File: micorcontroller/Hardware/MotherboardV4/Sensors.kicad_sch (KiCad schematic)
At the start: 36 parts, among them IC5 MS561101BA03-50, U1 TLV9002QDRQ1

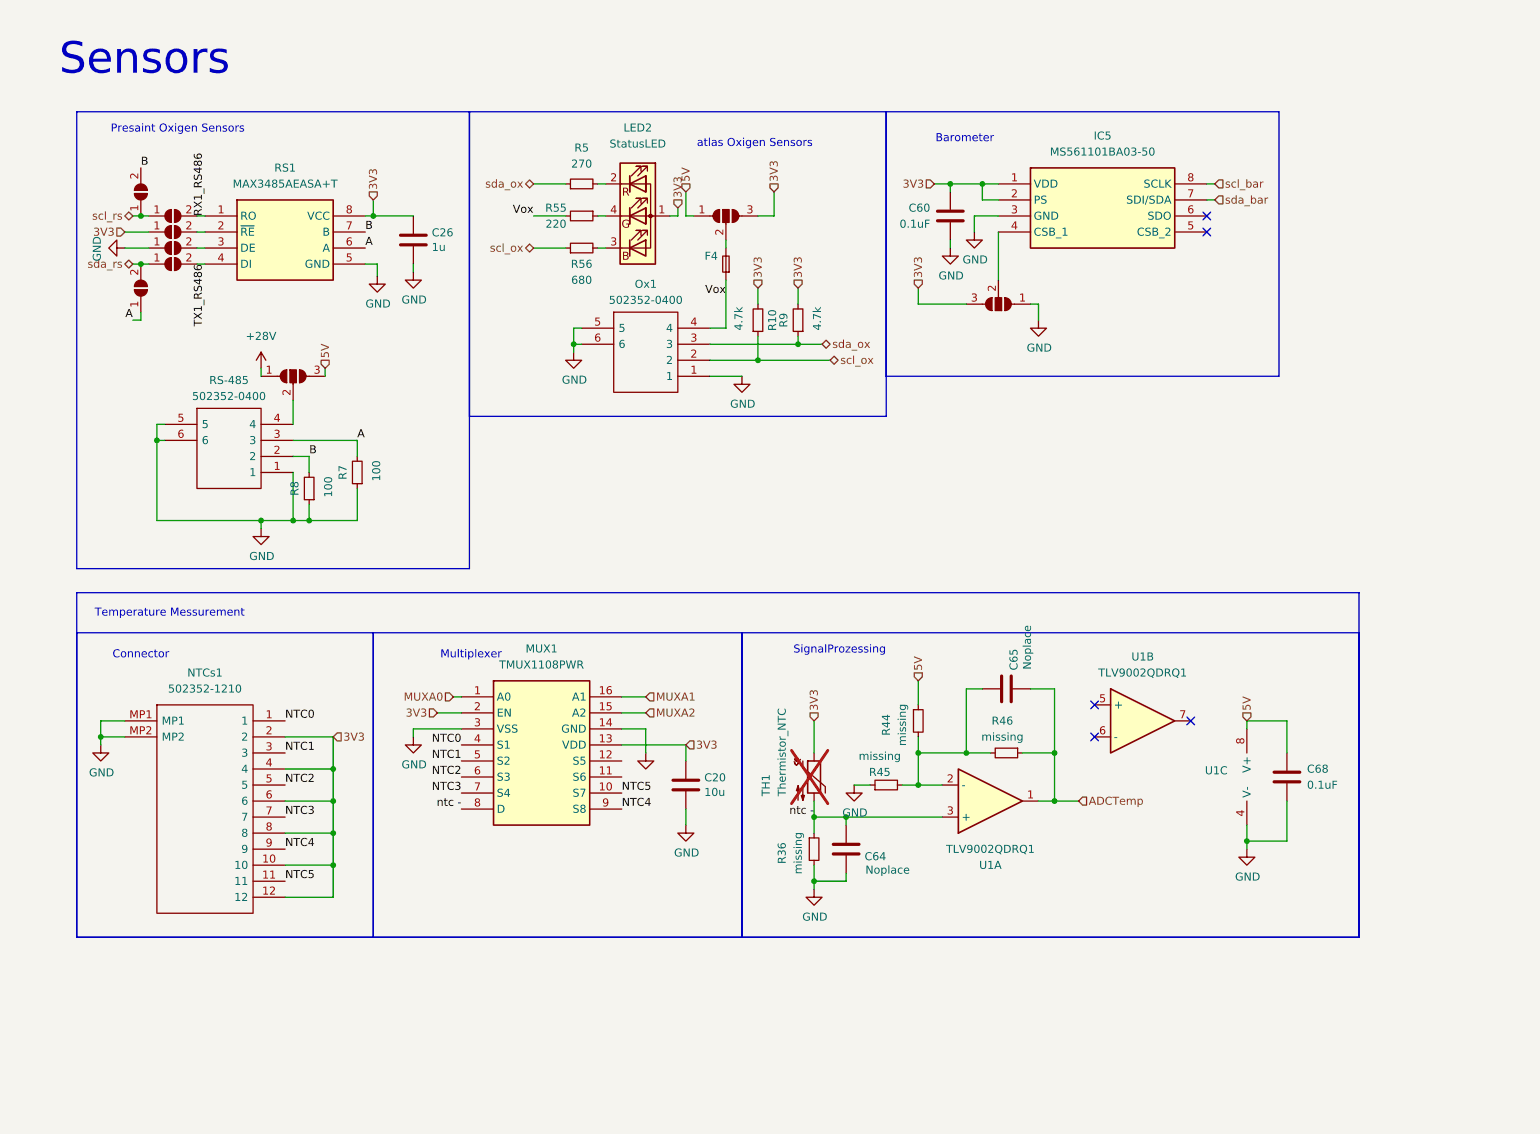
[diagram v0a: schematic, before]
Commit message: added NTC calculation
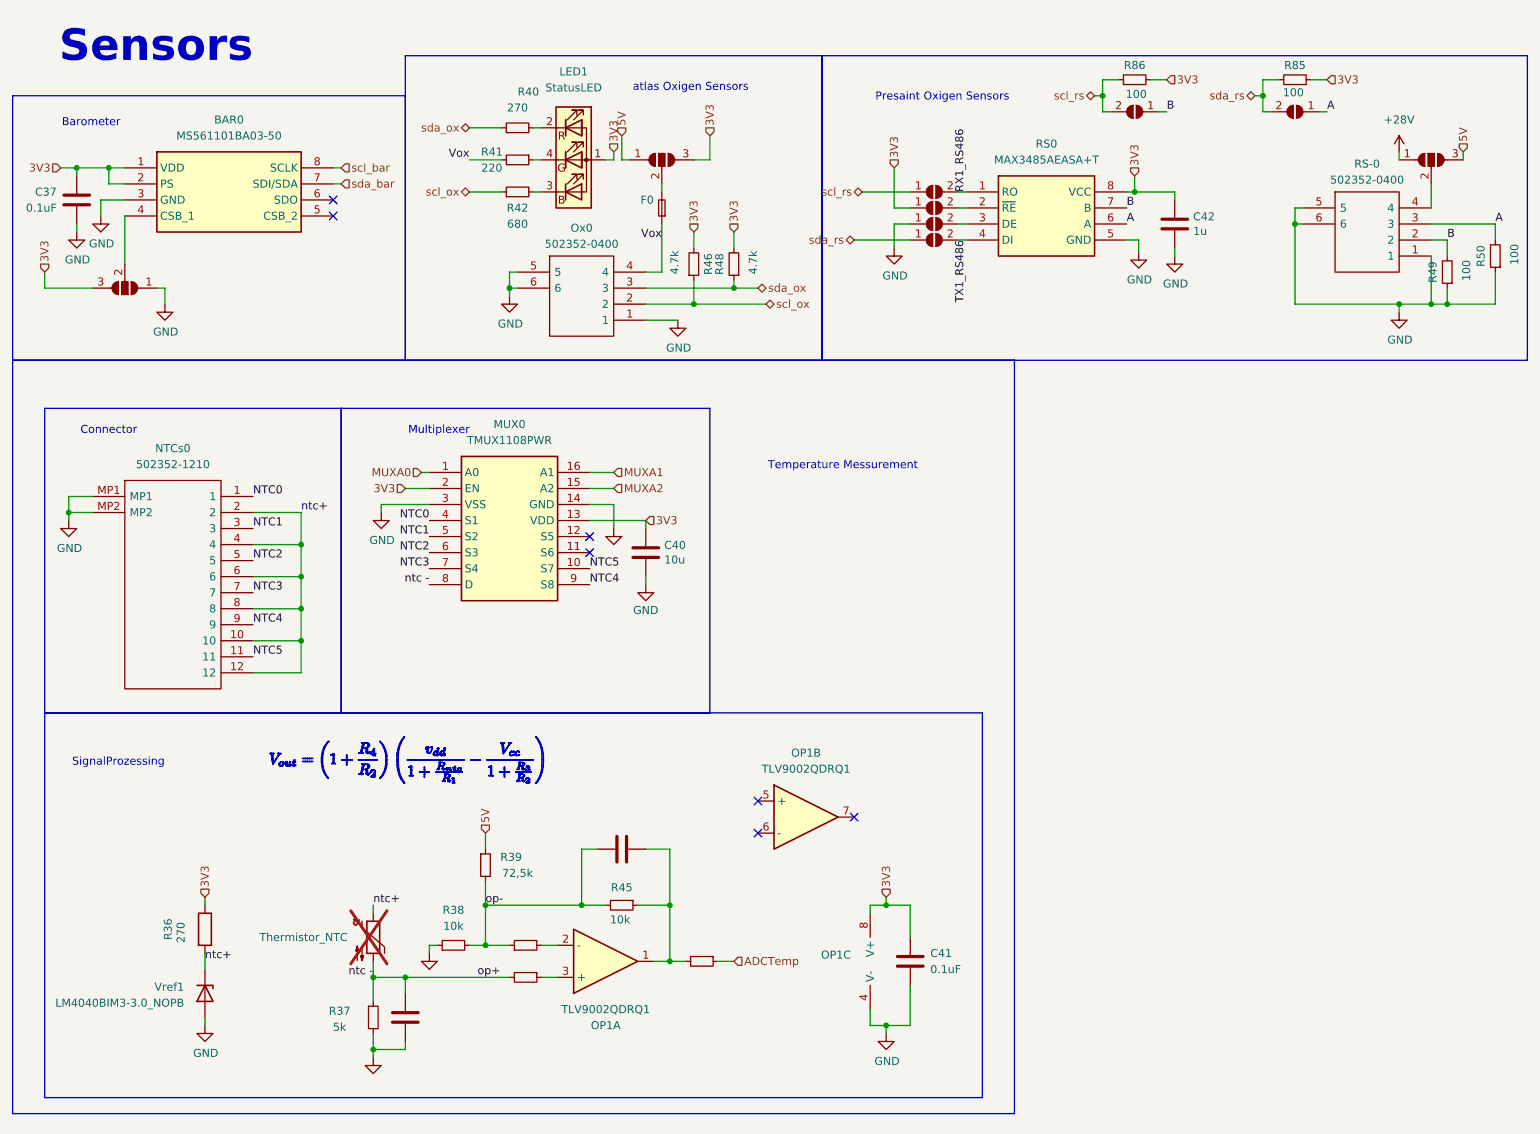
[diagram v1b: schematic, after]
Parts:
- added R36: 270, Resistor_SMD:R_0603_1608Metric_Pad0.98x0.95mm_HandSolder, symbol Device:R
- added R43, R44, R47: 1k, Resistor_SMD:R_0603_1608Metric_Pad0.98x0.95mm_HandSolder, symbol Device:R_Small
- added R85, R86: 100, Resistor_SMD:R_0603_1608Metric_Pad0.98x0.95mm_HandSolder, symbol Device:R_Small
- added Vref1: LM4040BIM3-3.0_NOPB, SamacSys_Parts:SOT95P237X112-3N, symbol Device:D_Zener
- C38: renamed from C64; value Noplace -> DNP
- C39: renamed from C65; value Noplace -> DNP
- R37: renamed from R36; value missing -> 5k
- R38: renamed from R45; value missing -> 10k
- R39: renamed from R44; value missing -> 72,5k
- R45: renamed from R46; value missing -> 10k
- renumbered IC5 to BAR0, C60 to C37, C20 to C40, C68 to C41, C26 to C42, F4 to F0, JP8 to JP3, JP9 to JP4, JP10 to JP5, JP1 to JP6, JP6 to JP7, JP11 to JP8, JP12 to JP9, JPVOX2 to JPVOX0, LED2 to LED1, MUX1 to MUX0, NTCs1 to NTCs0, U1 to OP1, Ox1 to Ox0, R5 to R40, R55 to R41, R56 to R42, R10 to R46, R9 to R48, R8 to R49, R7 to R50, RS-485 to RS-0, RS1 to RS0, TH1 to TH0
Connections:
- net 3V3: now also C41.2, OP1.8 (V+), R36.1, R85.1, R86.2; no longer NTCs0.10, NTCs0.12, NTCs0.2, NTCs0.4, NTCs0.6, NTCs0.8, TH0.1
- net 5V: no longer C41.2, OP1.8 (V+)
- net ADCTemp: now also R47.1; no longer C39.1, OP1.1, R45.1
- net B: now also JP3.1 (A); no longer JP3.2 (B)
- net GND: now also Vref1.2 (A)
- net ntc -: now also R44.2; no longer OP1.3 (+)
- net scl_rs: now also JP3.2 (B), R86.1; no longer JP3.1 (A)
- net sda_rs: now also R85.2
- net op-: now reaches C39.2, R38.2, R39.2, R45.2
- net op-: now also R43.1; no longer OP1.2 (-)
- new net: C39.1, OP1.1, R45.1, R47.2
- new net: OP1.2 (-), R43.2
- new net: OP1.3 (+), R44.1
- new net ntc+: NTCs0.10, NTCs0.12, NTCs0.2, NTCs0.4, NTCs0.6, NTCs0.8, R36.2, TH0.1, Vref1.1 (K)
- no-connect marks 5 -> 7
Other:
- moved on the sheet: BAR0, C37, C40, C41, C42, F0, LED1, MUX0, NTCs0, OP1A, OP1B, OP1C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

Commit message: propper Serial Comand System added
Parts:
- added R87: 10k, Resistor_SMD:R_0603_1608Metric_Pad0.98x0.95mm_HandSolder, symbol Device:R_Small
- added RT0: NTCGS163JF103FT8, THRMC1608X90N, symbol Device:Thermistor_NTC
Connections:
- net ntc+: now also R87.2, RT0.2
- net at MUX0.11 (S6): now also R87.1
- net at MUX0.12 (S5): now also RT0.1
- no-connect marks 7 -> 5
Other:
- moved on the sheet: C40

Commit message: added a serial command field for easy debugging
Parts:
- added R88: 0 DNP, Resistor_SMD:R_0603_1608Metric_Pad0.98x0.95mm_HandSolder, symbol Device:R_Small
- R37: value 5k -> 5.1k
- R39: value 72,5k -> 6,5k
- R85, R86: value 100 -> 4,7k
- RT0: footprint THRMC1608X90N -> SamacSys_Parts:THRMC1608X90N
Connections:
- net 5V: no longer R39.1
- net A: now also R49.2; no longer R50.2
- net ADCTemp: now also R88.1
- net B: now also R50.2; no longer R49.2
- net GND: now also RS-0.4; no longer RS-0.1
- net ntc -: now also R88.2
- net ntc+: now also R39.1
- net at JP9.2 (C): now also RS-0.1; no longer RS-0.4
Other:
- moved on the sheet: RS-0
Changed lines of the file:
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@@
 	)
 	(junction
-		(at 217.17 49.53)
+		(at 217.17 53.34)
+		(diameter 0)
+		(color 0 0 0 0)
+	)
+	(junction
+		(at 86.36 168.91)
 		(diameter 0)
 		(color 0 0 0 0)
@@
 	)
 	(junction
+		(at 127 166.37)
+		(diameter 0)
+		(color 0 0 0 0)
+	)
+	(junction
 		(at 128.27 59.69)
 		(diameter 0)
@@
 	(wire
 		(pts
-			(xy 147.32 52.07) (xy 156.21 52.07)
+			(xy 151.13 52.07) (xy 156.21 52.07)
 		)
 		(stroke
@@
 	(wire
 		(pts
-			(xy 217.17 46.99) (xy 217.17 49.53)
+			(xy 217.17 50.8) (xy 217.17 53.34)
 		)
 		(stroke
@@
 	(wire
 		(pts
-			(xy 218.44 46.99) (xy 217.17 46.99)
+			(xy 218.44 50.8) (xy 217.17 50.8)
 		)
 		(stroke
@@
 		)
 	)
+	(wire
+		(pts
+			(xy 127 180.34) (xy 127 166.37)
+		)
+		(stroke
+			(width 0)
+			(type default)
+		)
+	)
 	(polyline
 		(pts
@@
 	(wire
 		(pts
+			(xy 109.22 180.34) (xy 127 180.34)
+		)
+		(stroke
+			(width 0)
+			(type default)
+		)
+	)
+	(wire
+		(pts
 			(xy 118.11 166.37) (xy 115.57 166.37)
 		)
@@
 		)
 	)
+	(wire
+		(pts
+			(xy 86.36 168.91) (xy 86.36 180.34)
+		)
+		(stroke
+			(width 0)
+			(type default)
+		)
+	)
 	(polyline
 		(pts
@@
 		)
 	)
+	(wire
+		(pts
+			(xy 104.14 180.34) (xy 86.36 180.34)
+		)
+		(stroke
+			(width 0)
+			(type default)
+		)
+	)
 	(polyline
 		(pts
@@
 		)
 	)
+	(wire
+		(pts
+			(xy 127 166.37) (xy 128.27 166.37)
+		)
+		(stroke
+			(width 0)
+			(type default)
+		)
+	)
+	(wire
+		(pts
+			(xy 86.36 168.91) (xy 92.71 168.91)
+		)
+		(stroke
+			(width 0)
+			(type default)
+		)
+	)
 	(polyline
 		(pts
@@
 	(wire
 		(pts
-			(xy 238.76 52.07) (xy 241.3 52.07)
+			(xy 238.76 50.8) (xy 241.3 50.8)
 		)
 		(stroke
@@
 	(wire
 		(pts
-			(xy 148.59 44.45) (xy 156.21 44.45)
+			(xy 151.13 44.45) (xy 156.21 44.45)
 		)
 		(stroke
@@
 	(wire
 		(pts
-			(xy 238.76 43.18) (xy 238.76 46.99)
+			(xy 238.76 43.18) (xy 238.76 45.72)
 		)
 		(stroke
@@
 	(wire
 		(pts
-			(xy 248.92 52.07) (xy 248.92 49.53)
+			(xy 248.92 52.07) (xy 248.92 48.26)
 		)
 		(stroke
@@
 	(wire
 		(pts
-			(xy 241.3 54.61) (xy 241.3 52.07)
+			(xy 241.3 54.61) (xy 241.3 50.8)
 		)
 		(stroke
@@
 	(wire
 		(pts
-			(xy 125.73 166.37) (xy 128.27 166.37)
+			(xy 125.73 166.37) (xy 127 166.37)
 		)
 		(stroke
@@
 	(wire
 		(pts
-			(xy 238.76 49.53) (xy 248.92 49.53)
+			(xy 238.76 48.26) (xy 248.92 48.26)
 		)
 		(stroke
@@
 	(wire
 		(pts
-			(xy 238.76 54.61) (xy 238.76 62.23)
+			(xy 238.76 53.34) (xy 238.76 62.23)
 		)
 		(stroke
@@
 	(wire
 		(pts
-			(xy 76.2 168.91) (xy 92.71 168.91)
+			(xy 76.2 168.91) (xy 86.36 168.91)
 		)
 		(stroke
@@
 	(wire
 		(pts
-			(xy 217.17 49.53) (xy 218.44 49.53)
+			(xy 217.17 53.34) (xy 218.44 53.34)
 		)
 		(stroke
@@
 	(wire
 		(pts
-			(xy 217.17 49.53) (xy 217.17 62.23)
+			(xy 217.17 53.34) (xy 217.17 62.23)
 		)
 		(stroke
@@
 	)
 	(label "A"
-		(at 248.92 49.53 0)
+		(at 241.3 50.8 0)
 		(fields_autoplaced yes)
 		(effects
@@
 	)
 	(label "B"
-		(at 241.3 52.07 0)
+		(at 248.92 48.26 0)
 		(fields_autoplaced yes)
 		(effects
@@
 		)
 	)
+	(label "ntc+"
+		(at 88.9 146.05 0)
+		(fields_autoplaced yes)
+		(effects
+			(font
+				(size 1.27 1.27)
+			)
+			(justify left bottom)
+		)
+	)
 	(label "RX1_RS486"
 		(at 165.1 44.45 90)
@@
 		)
 	)
-	(hierarchical_label "5V"
-		(shape input)
-		(at 88.9 146.05 90)
-		(fields_autoplaced yes)
-		(effects
-			(font
-				(size 1.27 1.27)
-			)
-			(justify left)
-		)
-	)
 	(hierarchical_label "3V3"
 		(shape input)
@@
 	(hierarchical_label "sda_rs"
 		(shape bidirectional)
-		(at 147.32 52.07 180)
+		(at 151.13 52.07 180)
 		(fields_autoplaced yes)
 		(effects
@@
 	(hierarchical_label "scl_rs"
 		(shape bidirectional)
-		(at 148.59 44.45 180)
+		(at 151.13 44.45 180)
 		(fields_autoplaced yes)
 		(effects
@@
 			)
 		)
-		(property "Value" "72,5k"
+		(property "Value" "6,5k"
 			(at 93.98 152.4 0)
 			(effects
@@
 			)
 		)
-		(property "Value" "100"
+		(property "Value" "4,7k"
 			(at 216.916 28.702 90)
 			(effects
@@
 			)
 		)
-		(property "Footprint" "THRMC1608X90N"
+		(property "Footprint" "SamacSys_Parts:THRMC1608X90N"
 			(at 123.19 95.25 0)
 			(effects
@@
 	)
 	(symbol
+		(lib_id "Device:R_Small")
+		(at 106.68 180.34 270)
+		(unit 1)
+		(exclude_from_sim no)
+		(in_bom no)
+		(on_board yes)
+		(dnp yes)
+		(property "Reference" "R88"
+			(at 106.934 178.562 90)
+			(effects
+				(font
+					(size 1.27 1.27)
+				)
+				(hide yes)
+			)
+		)
+		(property "Value" "0 DNP"
+			(at 106.934 182.372 90)
+			(effects
+				(font
+					(size 1.27 1.27)
+				)
+				(hide yes)
+			)
+		)
+		(property "Footprint" "Resistor_SMD:R_0603_1608Metric_Pad0.98x0.95mm_HandSolder"
+			(at 106.68 180.34 0)
+			(effects
+				(font
+					(size 1.27 1.27)
+				)
+				(hide yes)
+			)
+		)
+		(property "Datasheet" "~"
+			(at 106.68 180.34 0)
+			(effects
+				(font
+					(size 1.27 1.27)
+				)
+				(hide yes)
+			)
+		)
+		(property "Description" "Resistor, small symbol"
+			(at 106.68 180.34 0)
+			(effects
+				(font
+					(size 1.27 1.27)
+				)
+				(hide yes)
+			)
+		)
+		(pin "2"
+		)
+		(pin "1"
+		)
+		(instances
+			(project "BalloonMotherboardV4"
+				(path "/a70d325c-f83f-4714-a2b6-4ef8919d016e/5e9e7f42-9819-4074-87ce-68c089720394"
+					(reference "R88")
+					(unit 1)
+				)
+			)
+		)
+	)
+	(symbol
 		(lib_id "Jumper:SolderJumper_3_Open")
 		(at 116.84 39.37 0)
@@
 			)
 		)
-		(property "Value" "100"
+		(property "Value" "4,7k"
 			(at 192.024 28.956 90)
 			(effects
@@
 			)
 		)
-		(property "Value" "5k"
+		(property "Value" "5.1k"
 			(at 65.786 176.784 0)
 			(effects
@@
 	(symbol
 		(lib_id "SamacSys_Parts:502352-0400")
-		(at 218.44 46.99 0)
+		(at 218.44 53.34 0)
+		(mirror x)
 		(unit 1)
 		(exclude_from_sim no)
@@
 		(dnp no)
 		(property "Reference" "RS-0"
-			(at 228.6 40.005 0)
+			(at 225.298 41.402 0)
 			(effects
 				(font
@@
 		)
 		(property "Value" "502352-0400"
-			(at 228.6 42.545 0)
+			(at 225.298 38.862 0)
 			(effects
 				(font
@@
 		)
 		(property "Footprint" "SamacSys_Parts:5023520400"
-			(at 234.95 44.45 0)
+			(at 234.95 55.88 0)
 			(effects
 				(font
@@
 		)
 		(property "Datasheet" "https://www.molex.com/webdocs/datasheets/pdf/en-us/5023520400_PCB_HEADERS.pdf"
-			(at 234.95 46.99 0)
+			(at 234.95 53.34 0)
 			(effects
 				(font
@@
 		)
 		(property "Description" "Molex DURACLIK 502352, 2mm Pitch, 4 Way, 1 Row, Right Angle PCB Header, Surface Mount"
-			(at 234.95 49.53 0)
+			(at 234.95 50.8 0)
 			(effects
 				(font
@@
 		)
 		(property "Height" "6"
-			(at 234.95 52.07 0)
+			(at 234.95 48.26 0)
 			(effects
 				(font
@@
 		)
 		(property "Mouser Part Number" "538-502352-0400"
-			(at 234.95 54.61 0)
+			(at 234.95 45.72 0)
 			(effects
 				(font
@@
 		)
 		(property "Mouser Price/Stock" "https://www.mouser.co.uk/ProductDetail/Molex/502352-0400?qs=trbuaetfxXR36zZJ3J6CsQ%3D%3D"
-			(at 234.95 57.15 0)
+			(at 234.95 43.18 0)
 			(effects
 				(font
@@
 		)
 		(property "Manufacturer_Name" "Molex"
-			(at 234.95 59.69 0)
+			(at 234.95 40.64 0)
 			(effects
 				(font
@@
 		)
 		(property "Manufacturer_Part_Number" "502352-0400"
-			(at 234.95 62.23 0)
+			(at 234.95 38.1 0)
 			(effects
 				(font

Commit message: Switch to header BASED C file system {headache incomming}
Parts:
- removed C38: DNP, Capacitor_SMD:C_0402_1005Metric_Pad0.74x0.62mm_HandSolder, symbol Device:C
- removed R88: 0 DNP, Resistor_SMD:R_0603_1608Metric_Pad0.98x0.95mm_HandSolder, symbol Device:R_Small
- added C41: DNP, Capacitor_SMD:C_0402_1005Metric_Pad0.74x0.62mm_HandSolder, symbol Device:C
- added R39, R40, R42, R44, R50, R51, R52, R54: 5.1k, Resistor_SMD:R_0603_1608Metric_Pad0.98x0.95mm_HandSolder, symbol Device:R_Small
- R38: renamed from R37; now not fitted; now left out of the parts list
- renumbered C37 to C40, C39 to C42, C41 to C43, C40 to C44, C42 to C45, JP5 to JP3, JP6 to JP4, JP7 to JP5, JP8 to JP6, JP3 to JP7, JP4 to JP8, R36 to R37, R38 to R41, R39 to R43, R40 to R45, R41 to R46, R42 to R47, R43 to R48, R44 to R49, R45 to R53, R46 to R55, R47 to R56, R48 to R57, R86 to R58, R85 to R59, R87 to R60, R49 to R61, R50 to R62
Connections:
- net 3V3: no longer C43.2, C44.1, MUX0.13 (VDD), MUX0.2 (EN), OP1.8 (V+), R37.1
- net 5V: no longer JPVOX1.1 (A)
- net GND: now also C41.1, R39.2, R40.2, R42.2, R44.2, R50.2, R51.2, R52.2, R54.2
- net NTC0: now also R39.1
- net NTC1: now also R40.1
- net NTC2: now also R42.1
- net NTC3: now also R44.1
- net NTC4: now also R50.1
- net NTC5: now also R51.1
- net ntc -: now also C41.2
- net NTC7: now reaches MUX0.11 (S6), R60.1
- net NTC7: now also R54.1
- net NTC6: now reaches MUX0.12 (S5), RT0.1
- net NTC6: now also R52.1
- new net 3V3uC: C43.2, C44.1, MUX0.13 (VDD), MUX0.2 (EN), OP1.8 (V+), R37.1
- new net BUCK: JPVOX1.1 (A)
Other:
- moved on the sheet: C44, LED1, MUX0, R45, R46, R47, R60, RT0

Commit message: startup message
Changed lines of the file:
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@@
 	)
 	(arc
-		(start 81.2439 132.6404)
-		(mid 81.244 132.6596)
-		(end 81.2369 132.6487)
+		(start 81.2369 132.6487)
+		(mid 81.2388 132.6431)
+		(end 81.2439 132.6404)
 		(stroke
 			(width 0.08)
@@
 	)
 	(arc
-		(start 95.35 138.0726)
-		(mid 95.3708 138.0738)
-		(end 95.3605 138.0844)
+		(start 95.3605 138.0844)
+		(mid 95.3514 138.0815)
+		(end 95.35 138.0726)
 		(stroke
 			(width 0.08)
@@
 	)
 	(arc
-		(start 85.0546 136.1217)
-		(mid 85.0391 136.1162)
-		(end 85.0477 136.107)
+		(start 85.0477 136.107)
+		(mid 85.0601 136.1115)
+		(end 85.0546 136.1217)
 		(stroke
 			(width 0.08)
@@
 	)
 	(arc
-		(start 82.4029 136.7281)
-		(mid 82.4004 136.7249)
-		(end 82.4032 136.7206)
+		(start 82.4032 136.7206)
+		(mid 82.4025 136.7221)
+		(end 82.4029 136.7281)
 		(stroke
 			(width 0.08)
@@
 	)
 	(arc
-		(start 94.281 135.9581)
-		(mid 94.2805 135.9581)
-		(end 94.28 135.9518)
+		(start 94.28 135.9518)
+		(mid 94.2839 135.9543)
+		(end 94.281 135.9581)
 		(stroke
 			(width 0.08)

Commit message: added uplink
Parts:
- BAR0: symbol SamacSys_Parts:MS561101BA03-50 -> SymbolsBalloonv4:MS561101BA03-50
- C40, C41, C42, C43, C44, C45: symbol Device:C -> SymbolsBalloonv4:C
- F0: symbol Device:Fuse_Small -> SymbolsBalloonv4:Fuse_Small
- JP3, JP4, JP5, JP6, JP7, JP8: symbol Jumper:SolderJumper_2_Open -> SymbolsBalloonv4:SolderJumper_2_Open
- JP9, JPVOX0, JPVOX1: symbol Jumper:SolderJumper_3_Open -> SymbolsBalloonv4:SolderJumper_3_Open
- LED1: symbol Device:LED_ARBG -> SymbolsBalloonv4:LED_ARBG
- MUX0: symbol SamacSys_Parts:TMUX1108PWR -> SymbolsBalloonv4:TMUX1108PWR
- NTCs0: symbol SamacSys_Parts:502352-1210 -> SymbolsBalloonv4:502352-1210
- OP1: symbol Device:Opamp_Dual -> SymbolsBalloonv4:Opamp_Dual
- Ox0, RS-0: symbol SamacSys_Parts:502352-0400 -> SymbolsBalloonv4:502352-0400
- R37: symbol Device:R -> SymbolsBalloonv4:R
- R38, R39, R40, R41, R42, R43, R44, R45, R46, R47, R48, R49, R50, R51, R52, R53, R54, R55, R56, R57, R58, R59, R60, R61, R62: symbol Device:R_Small -> SymbolsBalloonv4:R_Small
- RS0: symbol SamacSys_Parts:MAX3485AEASA+T -> SymbolsBalloonv4:MAX3485AEASA+T
- RT0, TH0: symbol Device:Thermistor_NTC -> SymbolsBalloonv4:Thermistor_NTC
- Vref1: symbol Device:D_Zener -> SymbolsBalloonv4:D_Zener
